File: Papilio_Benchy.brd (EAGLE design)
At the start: 101.6 x 55.9 mm, 137 parts, among them IC1 FT2232H, IC2 93C46, J1 USB MICRO, J4 HDMI-TYPE-A-RECEPTICALFCI1002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, SW1 SWITCH-2CH-6P-3010010P1, SW2 EVQQ2, T1 MOSFET-NCHANNELSMD, U1 ATMEGA32U4-XUMU, U11 PCA9306, U2 LTC3419EMS, U5 ARDUINO_MEGA_SHIELD, X2 12MHz, Y1 16MHz KX-7

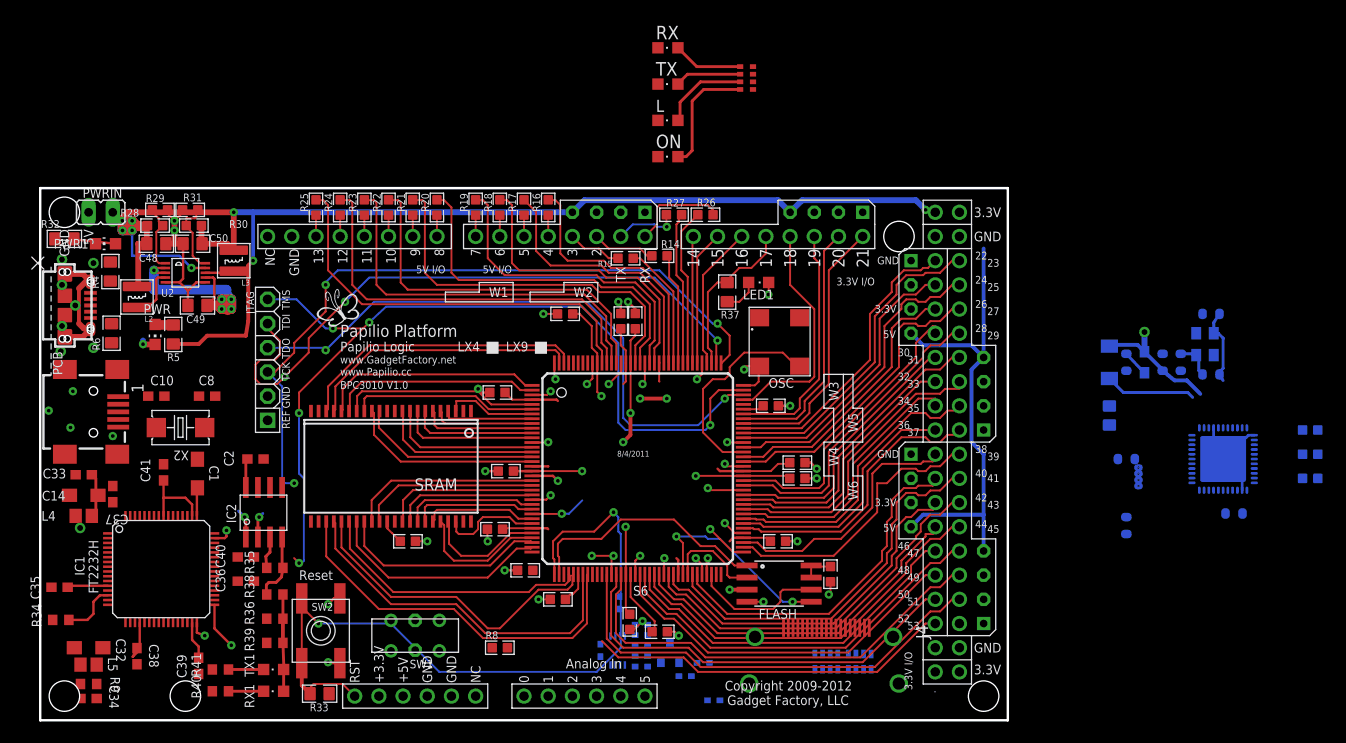
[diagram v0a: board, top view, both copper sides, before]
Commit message: Place and route FT2232H
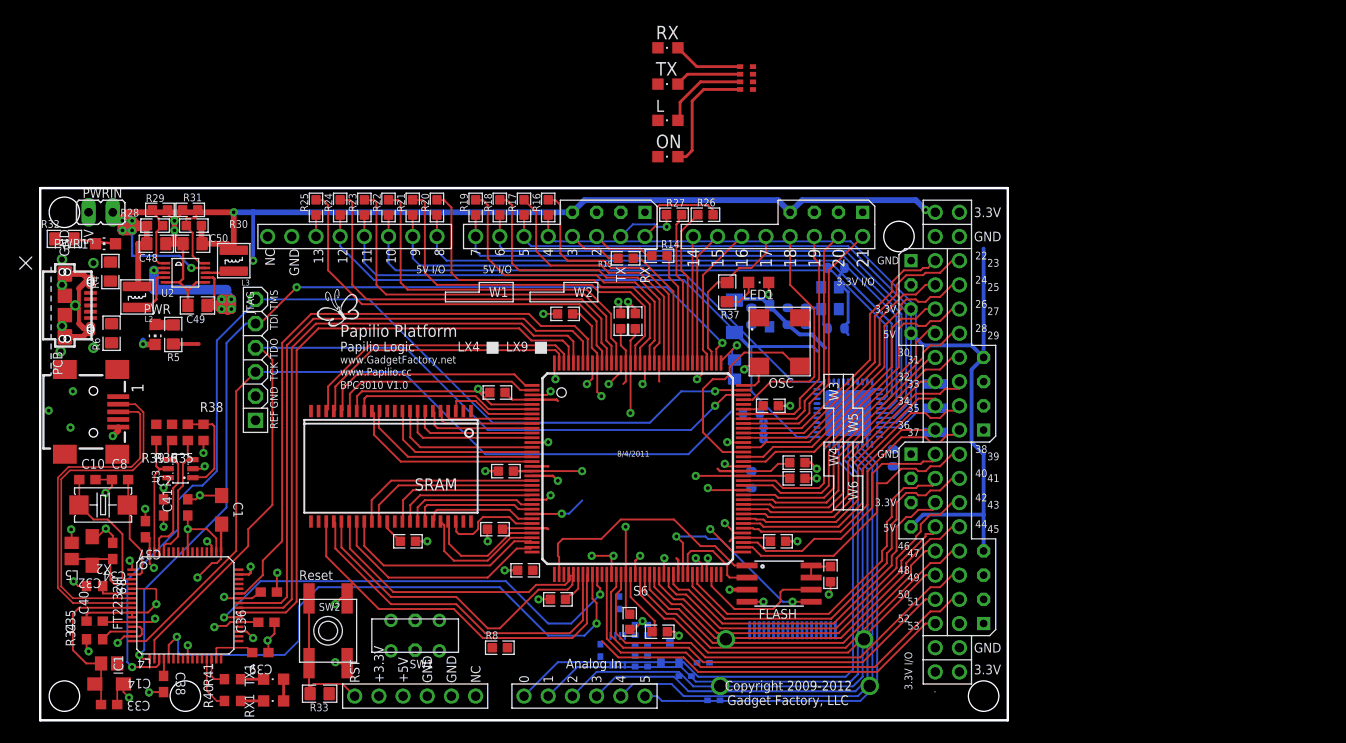
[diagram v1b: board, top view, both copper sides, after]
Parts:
- removed IC2: 93C46, dp_devices:SOIC8
- removed RN1, RN3: 51, saanlima:CTS742C083
- added U3: 93C46B, Bogdan_Commons:SOT23-6
- moved C11 39.7 mm to (83.6, 47.5)
- moved C5 39.7 mm to (74.7, 42.4)
- moved C6 39.7 mm to (74.7, 25.3)
- moved C7 39.7 mm to (74.7, 32.3)
- moved D2 39.7 mm to (72.9, 42.4)
- moved R1 39.7 mm to (83.6, 41.1)
- moved R2 39.7 mm to (75.9, 30.1)
- moved R3 39.7 mm to (75.9, 30.7)
- moved R7 39.7 mm to (72.9, 36.8)
- moved U1 39.7 mm to (84.8, 32.3)
- moved Y1 39.7 mm to (82.9, 44.3)
- moved C3 39.7 mm to (78.5, 42.4)
- moved C9 39.7 mm to (80.4, 42.4)
- moved L6 39.7 mm to (76.6, 42.4)
- moved R47 39.7 mm to (94.0, 35.3)
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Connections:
- net DM renamed FTUSB_N
- net DP renamed FTUSB_P
- removed net 3.3V: C2.1, C38.1, C39.1, C40.1, C41.1, IC1.20, IC1.31, IC1.42, IC1.50, IC1.56, IC2.6, IC2.8, L4.2, L5.2, R34.1, R36.2, R38.2, R39.2, RX1.A, TX1.A
- net 3V3: now also C2.1, C38.1, C39.1, C40.1, C41.1, IC1.20, IC1.31, IC1.42, IC1.50, IC1.56, L4.2, L5.2, R34.1, R36.2, R38.2, R39.2, RX1.A, TX1.A, U3.6; no longer RN1.5, RN1.6, RN1.7, RN1.8, RN3.5, RN3.6, RN3.7, RN3.8
- net ATMEGA_A0: now also U1.41; no longer U1.36
- net ATMEGA_A1: now also U1.40; no longer U1.37
- net ATMEGA_A2: now also U1.39; no longer U1.38
- net ATMEGA_A3: now also U1.38; no longer U1.39
- net ATMEGA_A4: now also U1.37; no longer U1.40
- net ATMEGA_A5: now also U1.36; no longer U1.41
- net ATMEGA_D4: now also U1.31; no longer U1.25
- net ATMEGA_D5*: now also U1.30; no longer U1.31
- net ATMEGA_D6*: now also U1.29; no longer U1.27
- net ATMEGA_D7: now also U1.28; no longer U1.1
- net ATMEGA_IO10*: now also U1.25; no longer U1.30
- net ATMEGA_IO12: now also U1.1; no longer U1.26
- net ATMEGA_IO8: now also U1.27; no longer U1.28
- net ATMEGA_IO9*: now also U1.26; no longer U1.29
- net BD1_MPSSE_TDI: now also S6.141; no longer S6.140
- net BD2_MPSSE_TDO: now also S6.140; no longer S6.141
- net EECLK: now also U3.4; no longer IC2.2
- net EECS: now also U3.5; no longer IC2.1
- net EEDATA: now also U3.3; no longer IC2.3
- net GND: now also U3.2; no longer IC2.5
- net MEGA_D45: no longer RN1.4
- net MEGA_D46: no longer RN1.3
- net MEGA_D47: no longer RN1.2
- net MEGA_D48: no longer RN1.1
- net MEGA_D49: no longer RN3.2
- net MEGA_D50: no longer RN3.1
- net MEGA_D51: no longer RN3.4
- net MEGA_D52: no longer RN3.3
- net N$45: now also U3.1; no longer IC2.4
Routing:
- net BD3_MPSSE_TMS: track 0.00 -> 67.2 mm
- net ATMEGA_IO10*: track 2.25 -> 68.4 mm
- net BD2_MPSSE_TDO: track 0.00 -> 66.0 mm
- net BD4-DTR: track 0.00 -> 65.5 mm
- net BD1_MPSSE_TDI: track 0.00 -> 65.0 mm
- net ATMEGA_IO9*: track 2.25 -> 66.9 mm
- net RESET: track 80.7 -> 16.1 mm, vias 2 -> 0
- net ATMEGA_IO8: track 2.25 -> 65.9 mm
- net ATMEGA_IO12: track 2.25 -> 64.3 mm
- net AD4-DTR: track 0.00 -> 61.4 mm, vias 0 -> 2
- net ATMEGA_A0: track 0.00 -> 61.2 mm
- net ATMEGA_D7: track 2.25 -> 63.3 mm
- net ATMEGA_D6*: track 2.25 -> 62.0 mm
- net ATMEGA_A1: track 0.00 -> 59.5 mm
- net ATMEGA_D5*: track 2.25 -> 60.6 mm
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- added copper zone on layer 3, net 1.8V

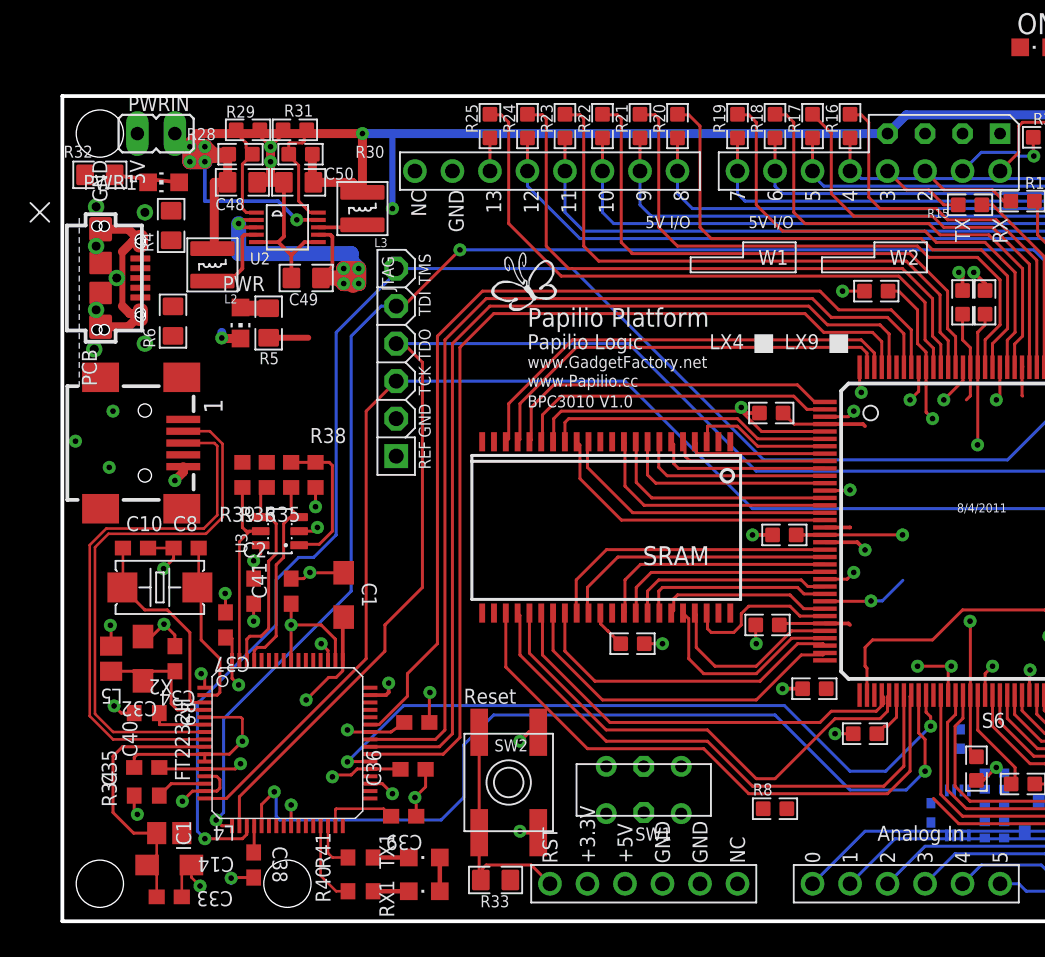
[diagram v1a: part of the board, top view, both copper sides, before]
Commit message: Power Supply PAR'd
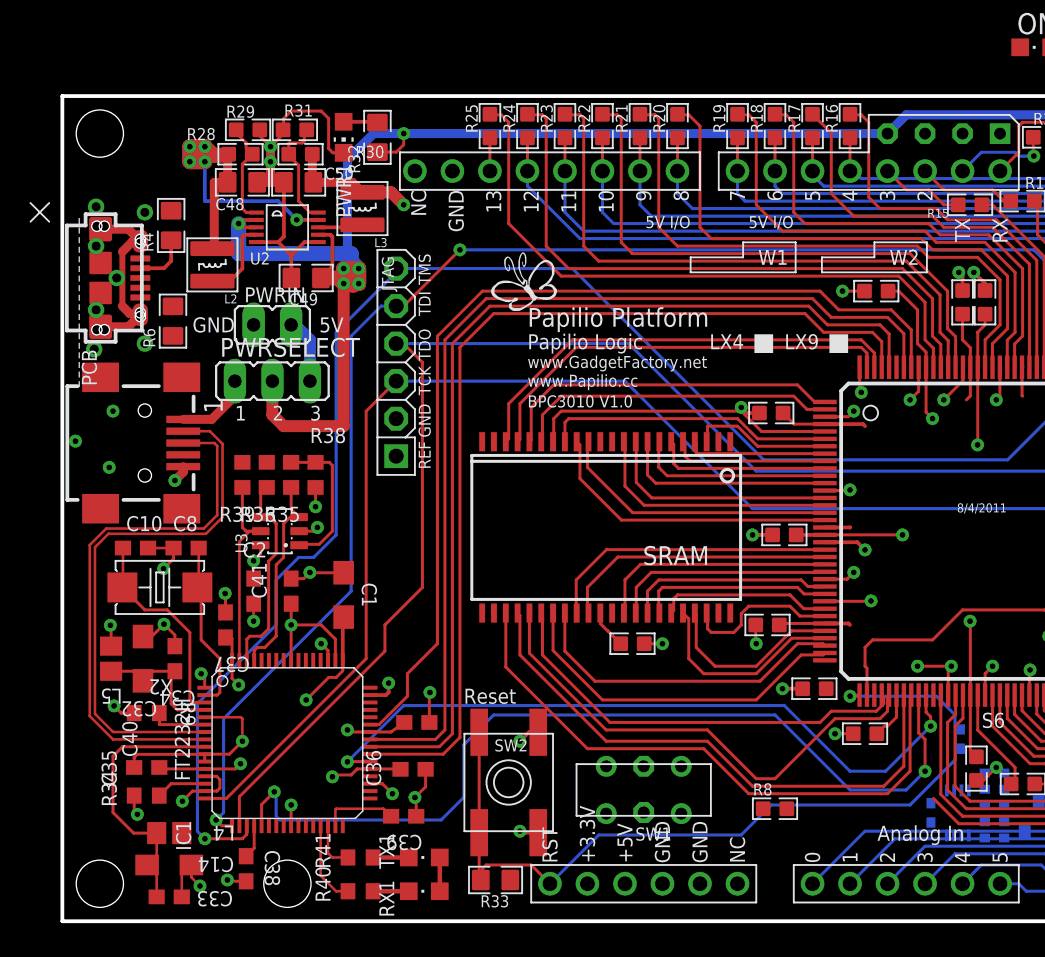
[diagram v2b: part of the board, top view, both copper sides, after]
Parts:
- removed PWR: (no value), led:CHIP-LED0805
- removed R5: 1K8, GadgetFactory:0805
- added PWRSELECT: (no value), jumper:JP2
- moved R32 19.0 mm to (21.3, 53.1), turned to 270 degrees
- moved PWRIN 15.2 mm to (14.2, 40.4)
- moved PWR1 12.6 mm to (19.1, 53.1), turned to 180 degrees
- moved C38 0.57 mm to (12.4, 3.56)
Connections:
- removed net 5V: C49.2, CONN1.VUSB, R11.2, R32.2, U2.2, U2.3, U2.7
- removed net N$1: PWR.A, R5.1
- new net VBUS_A: CONN1.VUSB, PWRSELECT.1
- net 5V0: now also C49.2, PWRSELECT.2, R11.2, R32.2, U2.2, U2.3, U2.7; no longer R5.2
- net GND: no longer PWR.C
- net VI: now also PWRSELECT.3
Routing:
- net 5V0: track 148.5 -> 226.1 mm, vias 3 -> 7
- net 1V2: track 48.1 -> 100.1 mm, vias 5 -> 6
- net RESET: track 16.1 -> 58.3 mm, vias 0 -> 1
- net 5V: track 27.6 -> 0.00 mm, vias 5 -> 0
- net VBUS_A: track 0.00 -> 5.16 mm
- net GND: track 172.3 -> 177.4 mm, vias 69 -> 68
- net VI: track 0.00 -> 4.48 mm
- net D-: track 0.00 -> 3.70 mm
- net N$8: track 4.41 -> 2.31 mm
- net N$1: track 1.96 -> 0.00 mm

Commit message: SRAM Cleaned up
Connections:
- net VBUS_A renamed 5V_FT2232
- net XUSB renamed 5V_ARDUINO
- net 5V0: now also PWRIN.1
- net VI: no longer PWRIN.1
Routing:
- net 5V_FT2232: track 5.16 -> 4.15 mm
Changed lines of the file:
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@@
 <layer number="1" name="Top" color="4" fill="1" visible="yes" active="yes"/>
 <layer number="2" name="Route2" color="6" fill="1" visible="no" active="yes"/>
-<layer number="3" name="Route3" color="4" fill="3" visible="yes" active="yes"/>
+<layer number="3" name="Route3" color="4" fill="3" visible="no" active="yes"/>
 <layer number="14" name="Route14" color="1" fill="6" visible="no" active="no"/>
 <layer number="15" name="Route15" color="5" fill="1" visible="no" active="no"/>
@@
 <layer number="17" name="Pads" color="2" fill="1" visible="yes" active="yes"/>
 <layer number="18" name="Vias" color="2" fill="1" visible="yes" active="yes"/>
-<layer number="19" name="Unrouted" color="12" fill="1" visible="no" active="yes"/>
+<layer number="19" name="Unrouted" color="12" fill="1" visible="yes" active="yes"/>
 <layer number="20" name="Dimension" color="15" fill="1" visible="yes" active="yes"/>
 <layer number="21" name="tPlace" color="25" fill="1" visible="yes" active="yes"/>
@@
 <layer number="23" name="tOrigins" color="15" fill="1" visible="yes" active="yes"/>
 <layer number="24" name="bOrigins" color="15" fill="1" visible="yes" active="yes"/>
-<layer number="25" name="tNames" color="7" fill="1" visible="no" active="yes"/>
+<layer number="25" name="tNames" color="7" fill="1" visible="yes" active="yes"/>
 <layer number="26" name="bNames" color="7" fill="1" visible="no" active="yes"/>
 <layer number="27" name="tValues" color="7" fill="1" visible="no" active="yes"/>
@@
 <wire x1="34.29" y1="16.002" x2="14.224" y2="36.068" width="0.2032" layer="3"/>
 <wire x1="14.224" y1="36.068" x2="14.224" y2="36.576" width="0.2032" layer="3"/>
+<contactref element="PWRIN" pad="1"/>
 <wire x1="92.964" y1="53.594" x2="99.06" y2="49.53" width="0" layer="19" extent="16-16"/>
+<wire x1="15.494" y1="40.386" x2="17.51" y2="43.561" width="0" layer="19" extent="1-1"/>
 <wire x1="68.3748" y1="4.64" x2="91.44" y2="20.32" width="0" layer="19" extent="16-16"/>
 </signal>
@@
 </signal>
 <signal name="VI">
-<contactref element="PWRIN" pad="1"/>
 <contactref element="PWRSELECT" pad="3"/>
-<wire x1="15.494" y1="40.386" x2="15.748" y2="40.386" width="0.8128" layer="16"/>
 <wire x1="15.748" y1="40.386" x2="16.764" y2="39.37" width="0.8128" layer="16"/>
 <wire x1="16.764" y1="39.37" x2="16.764" y2="36.576" width="0.8128" layer="16"/>
@@
 <wire x1="73.787" y1="32.258" x2="75.946" y2="31.3586" width="0" layer="19" extent="16-16"/>
 </signal>
-<signal name="XUSB" class="3">
+<signal name="5V_ARDUINO" class="3">
 <contactref element="J1" pad="P1"/>
 </signal>
@@
 <wire x1="81.561" y1="34.758" x2="93.18" y2="35.306" width="0" layer="19" extent="16-16"/>
 </signal>
-<signal name="VBUS_A">
-<contactref element="PWRSELECT" pad="1"/>
+<signal name="5V_FT2232">
 <contactref element="CONN1" pad="VUSB"/>
 <wire x1="8.188" y1="33.985" x2="10.109" y2="33.985" width="0.6096" layer="1"/>
 <wire x1="10.109" y1="33.985" x2="11.684" y2="35.56" width="0.6096" layer="1"/>
-<wire x1="11.684" y1="35.56" x2="11.684" y2="36.576" width="0.6096" layer="1"/>
+<contactref element="PWRSELECT" pad="1"/>
+<wire x1="11.684" y1="35.56" x2="11.684" y2="36.576" width="0" layer="19" extent="1-1"/>
 </signal>
 </signals>

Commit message: Before connecting Avr JTAG
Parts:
- removed D2: CD1206-S01575, diode:MINIMELF
- removed R47, R48, R49: 390, GadgetFactory:0603
- removed R7: 10K, GadgetFactory_6.0:0805
- C11, C3, C4, C5, C6, C7, C9: device SmartPrj:C0603-ROUND -> SmartPrj:C0603K
- moved J4 48.7 mm to (126.0, 21.2)
- moved C20 47.9 mm to (106.6, 10.9)
- moved R12 47.9 mm to (110.9, 13.6)
- moved R13 47.9 mm to (110.9, 12.5)
- moved R42 47.9 mm to (110.9, 10.3)
- moved R43 47.9 mm to (110.9, 9.20)
- moved R44 47.9 mm to (110.9, 11.4)
- moved R46 47.9 mm to (108.6, 15.9)
- moved U11 47.9 mm to (108.4, 10.9)
- moved R10 47.9 mm to (118.5, 5.66)
- moved R11 47.9 mm to (115.5, 8.20)
- moved R45 47.9 mm to (117.4, 9.60)
- moved T1 47.9 mm to (113.9, 10.6)
- moved R2 36.8 mm to (112.8, 29.1)
- moved R3 36.8 mm to (112.8, 29.7)
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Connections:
- removed net +5V: C3.1, C4.1, D2.C, L6.1, R7.2, RN2.1, RN2.3, RN2.4, U1.14, U1.2, U1.34
- removed net N$10: R49.2, U1.9
- removed net N$11: R48.2, U1.10
- removed net N$12: R47.2, U1.11
- removed net VI: PWRSELECT.3
- net 5V0: now also C3.1, C4.1, L6.1, RN2.1, RN2.3, RN2.4, U1.13, U1.14, U1.2, U1.34
- net 5V_ARDUINO: now also PWRSELECT.3
- net ARD_RESET: no longer D2.A, R7.1, U1.13
- net MEGA_D40: no longer R47.1
- net MEGA_D41: no longer R48.1
- net MEGA_D42: no longer R49.1
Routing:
- net ATMEGA_IO12: track 64.3 -> 2.25 mm
- net ATMEGA_IO11*: track 58.5 -> 46.6 mm
- net +5V: track 11.7 -> 0.00 mm
- net 5V_ARDUINO: track 0.00 -> 9.66 mm, vias 0 -> 1
- net ARD_RESET: track 9.56 -> 0.00 mm
- net ATMEGA_A1: track 59.5 -> 50.3 mm
- net ATMEGA_A0: track 61.2 -> 52.2 mm
- net ATMEGA_A3: track 55.7 -> 47.3 mm
- net ATMEGA_A2: track 57.6 -> 49.1 mm
- net 5V0: track 226.1 -> 231.9 mm
- net XTAL1: track 8.48 -> 14.3 mm
- net AREF: track 0.00 -> 5.64 mm
- net XTAL2: track 4.05 -> 9.02 mm
- net UCAP: track 0.00 -> 4.81 mm
- net A19: track 40.4 -> 35.6 mm
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- added copper zone on layer 3, net AVCC
